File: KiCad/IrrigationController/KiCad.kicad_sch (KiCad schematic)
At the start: 115 parts, among them IC1 MCP23017-E_SO, IC2 MCP23017-E_SO, IC3 DS89C21TMX_NOPB, J1 Screw_Terminal_01x03, J10 Screw_Terminal_01x05, J11 Screw_Terminal_01x02, J12 Screw_Terminal_01x02, J13 Screw_Terminal_01x04, J14 Screw_Terminal_01x02, J15 Screw_Terminal_01x02, J16 Screw_Terminal_01x02, J17 Screw_Terminal_01x02, J18 Screw_Terminal_01x02, J19 Screw_Terminal_01x02, J2 Screw_Terminal_01x03, J21 Screw_Terminal_01x06, J3 Screw_Terminal_01x03, J5 Screw_Terminal_01x03, J6 Screw_Terminal_01x02, J7 Screw_Terminal_01x02, J8 Screw_Terminal_01x02, J9 Screw_Terminal_01x02, K1 2071556-9, K2 2071556-9, Q1 MMBT3906, Q11 MMBT3904, Q12 MMBT3904, Q2 MMBT3906, Q3 MMBT3906, Q6 MMBT3904, Q7 MMBT3904, Q8 MMBT3904, SW1 SW_Push, U1 L298P, U2 ARDUINO_MKR_WAN_1310, U3 L298P, U4 L298P, U5 L298P, U7 L7805

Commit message: PCB created
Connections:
- net COM_1: now also J15.1 (Pin_1); no longer J15.2 (Pin_2)
- net COM_2: now also J16.1 (Pin_1); no longer J16.2 (Pin_2)
- net NO_1: now also J15.2 (Pin_2); no longer J15.1 (Pin_1)
- net NO_2: now also J16.2 (Pin_2); no longer J16.1 (Pin_1)
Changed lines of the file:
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@@
     (effects (font (size 1.27 1.27)) (justify left bottom))
-  )
-  (label "COM_1" (at 384.81 34.29 270) (fields_autoplaced)
-    (effects (font (size 1.27 1.27)) (justify right bottom))
   )
   (label "W2_IN1" (at 120.65 247.65 0) (fields_autoplaced)
@@
     (effects (font (size 1.27 1.27)) (justify left bottom))
   )
+  (label "NO_1" (at 384.81 34.29 270) (fields_autoplaced)
+    (effects (font (size 1.27 1.27)) (justify right bottom))
+  )
   (label "R1_EN" (at 85.09 240.03 180) (fields_autoplaced)
     (effects (font (size 1.27 1.27)) (justify right bottom))
@@
     (effects (font (size 1.27 1.27)) (justify left bottom))
   )
-  (label "COM_2" (at 400.05 34.29 270) (fields_autoplaced)
-    (effects (font (size 1.27 1.27)) (justify right bottom))
-  )
   (label "COM_2" (at 170.18 269.24 0) (fields_autoplaced)
     (effects (font (size 1.27 1.27)) (justify left bottom))
@@
     (effects (font (size 1.27 1.27)) (justify right bottom))
   )
+  (label "COM_2" (at 397.51 34.29 270) (fields_autoplaced)
+    (effects (font (size 1.27 1.27)) (justify right bottom))
+  )
   (label "P1_IN1" (at 328.93 132.08 90) (fields_autoplaced)
     (effects (font (size 1.27 1.27)) (justify left bottom))
@@
     (effects (font (size 1.27 1.27)) (justify right bottom))
   )
-  (label "NO_1" (at 382.27 34.29 270) (fields_autoplaced)
-    (effects (font (size 1.27 1.27)) (justify right bottom))
-  )
   (label "D0-" (at 269.24 275.59 180) (fields_autoplaced)
     (effects (font (size 1.27 1.27)) (justify right bottom))
@@
     (effects (font (size 1.27 1.27)) (justify right bottom))
   )
-  (label "NO_2" (at 397.51 34.29 270) (fields_autoplaced)
-    (effects (font (size 1.27 1.27)) (justify right bottom))
-  )
   (label "PULSE_IN" (at 110.49 49.53 0) (fields_autoplaced)
     (effects (font (size 1.27 1.27)) (justify left bottom))
@@
     (effects (font (size 1.27 1.27)) (justify right bottom))
   )
+  (label "NO_2" (at 400.05 34.29 270) (fields_autoplaced)
+    (effects (font (size 1.27 1.27)) (justify right bottom))
+  )
   (label "RELAY_2_EN" (at 120.65 242.57 0) (fields_autoplaced)
     (effects (font (size 1.27 1.27)) (justify left bottom))
@@
     (effects (font (size 1.27 1.27)) (justify left bottom))
   )
+  (label "COM_1" (at 382.27 34.29 270) (fields_autoplaced)
+    (effects (font (size 1.27 1.27)) (justify right bottom))
+  )
   (label "SDA" (at 91.44 54.61 0) (fields_autoplaced)

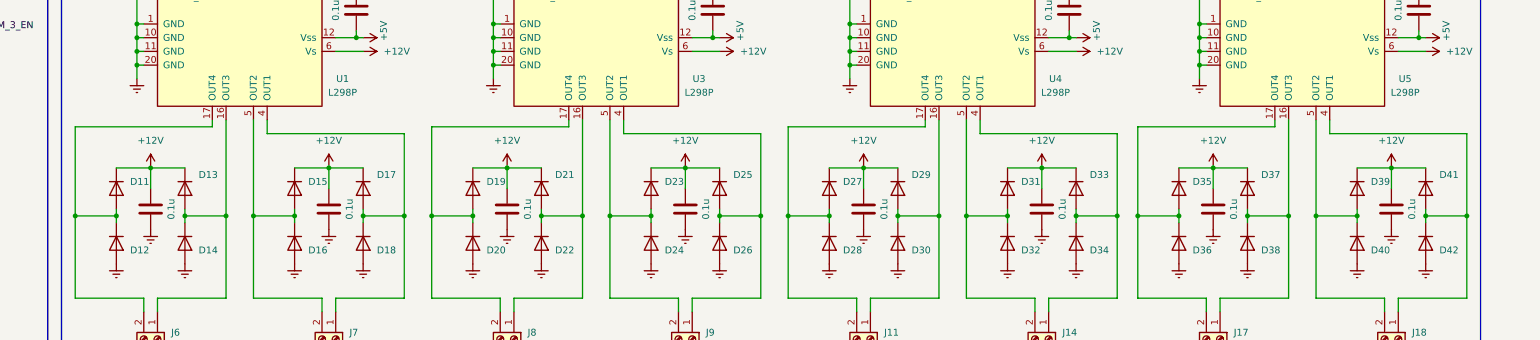
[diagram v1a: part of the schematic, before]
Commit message: L298 as Power
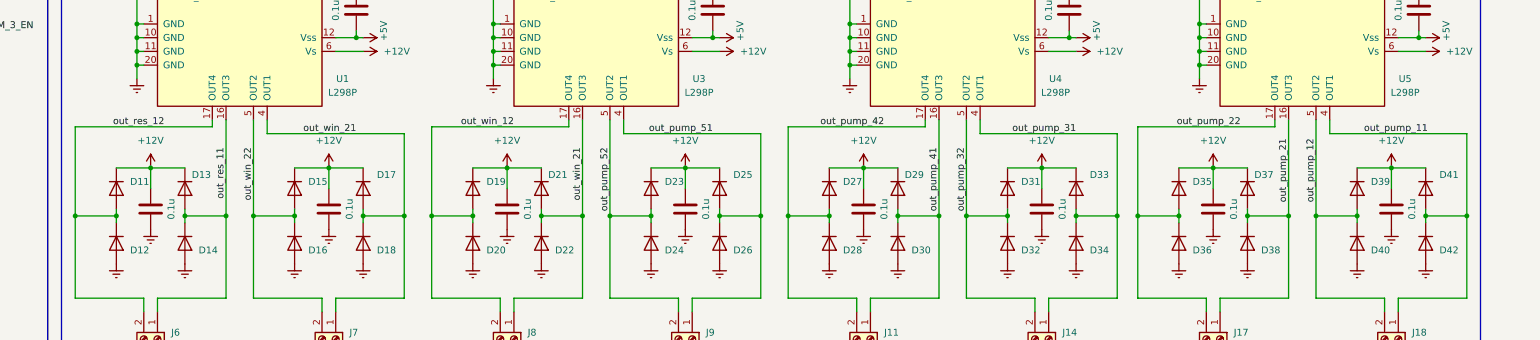
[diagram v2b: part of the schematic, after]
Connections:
- net out_pump_41: now reaches D29.2 (A), D30.1 (K), J11.1 (Pin_1), U4.16 (OUT3)
- net out_win_21: now reaches D17.2 (A), D18.1 (K), J7.1 (Pin_1), U1.4 (OUT1)
- net out_win_21: now also D21.2 (A), D22.1 (K), J8.1 (Pin_1), U3.16 (OUT3)
- net out_win_22: now reaches D15.2 (A), D16.1 (K), J7.2 (Pin_2), U1.5 (OUT2)
- net out_pump_21: now reaches D37.2 (A), D38.1 (K), J17.1 (Pin_1), U5.16 (OUT3)
- net out_win_12: now reaches D19.2 (A), D20.1 (K), J8.2 (Pin_2), U3.17 (OUT4)
- net out_pump_11: now reaches D41.2 (A), D42.1 (K), J18.1 (Pin_1), U5.4 (OUT1)
- net out_res_11: now reaches D13.2 (A), D14.1 (K), J6.1 (Pin_1), U1.16 (OUT3)
- net out_pump_12: now reaches D39.2 (A), D40.1 (K), J18.2 (Pin_2), U5.5 (OUT2)
- net out_pump_22: now reaches D35.2 (A), D36.1 (K), J17.2 (Pin_2), U5.17 (OUT4)
- net out_res_12: now reaches D11.2 (A), D12.1 (K), J6.2 (Pin_2), U1.17 (OUT4)
- net out_pump_42: now reaches D27.2 (A), D28.1 (K), J11.2 (Pin_2), U4.17 (OUT4)
- net out_pump_51: now reaches D25.2 (A), D26.1 (K), J9.1 (Pin_1), U3.4 (OUT1)
- net out_pump_52: now reaches D23.2 (A), D24.1 (K), J9.2 (Pin_2), U3.5 (OUT2)
- net out_pump_32: now reaches D31.2 (A), D32.1 (K), J14.2 (Pin_2), U4.5 (OUT2)
- net out_pump_31: now reaches D33.2 (A), D34.1 (K), J14.1 (Pin_1), U4.4 (OUT1)
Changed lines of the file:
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@@
     (stroke (width 0) (type default))
   )
-  (wire (pts (xy 323.85 170.18) (xy 349.25 170.18))
-    (stroke (width 0) (type default))
-  )
   (wire (pts (xy 240.03 240.03) (xy 240.03 241.3))
     (stroke (width 0) (type default))
@@
     (stroke (width 0) (type default))
   )
+  (wire (pts (xy 316.23 167.64) (xy 316.23 185.42))
+    (stroke (width 0) (type default))
+  )
   (wire (pts (xy 234.95 144.78) (xy 236.22 144.78))
     (stroke (width 0) (type default))
@@
     (stroke (width 0) (type default))
   )
-  (wire (pts (xy 218.44 200.66) (xy 205.74 200.66))
+  (wire (pts (xy 323.85 170.18) (xy 349.25 170.18))
     (stroke (width 0) (type default))
   )
-  (wire (pts (xy 256.54 167.64) (xy 256.54 185.42))
+  (wire (pts (xy 218.44 200.66) (xy 205.74 200.66))
     (stroke (width 0) (type default))
   )
@@
     (stroke (width 0) (type default))
   )
-  (wire (pts (xy 316.23 167.64) (xy 316.23 185.42))
-    (stroke (width 0) (type default))
-  )
   (wire (pts (xy 203.2 29.21) (xy 201.93 29.21))
     (stroke (width 0) (type default))
@@
     (stroke (width 0) (type default))
   )
+  (wire (pts (xy 256.54 167.64) (xy 256.54 185.42))
+    (stroke (width 0) (type default))
+  )
   (wire (pts (xy 124.46 185.42) (xy 124.46 200.66))
     (stroke (width 0) (type default))
@@
     (effects (font (size 1.27 1.27)) (justify left bottom))
   )
+  (label "out_pump_41" (at 251.46 172.72 270) (fields_autoplaced)
+    (effects (font (size 1.27 1.27)) (justify right bottom))
+  )
   (label "P5_EN" (at 62.23 247.65 0) (fields_autoplaced)
     (effects (font (size 1.27 1.27)) (justify left bottom))
@@
     (effects (font (size 1.27 1.27)) (justify left bottom))
   )
+  (label "out_pump_22" (at 307.34 168.91 180) (fields_autoplaced)
+    (effects (font (size 1.27 1.27)) (justify right bottom))
+  )
   (label "RI+" (at 307.34 36.83 90) (fields_autoplaced)
     (effects (font (size 1.27 1.27)) (justify left bottom))
@@
     (effects (font (size 1.27 1.27)) (justify right bottom))
   )
+  (label "out_pump_31" (at 276.86 170.18 180) (fields_autoplaced)
+    (effects (font (size 1.27 1.27)) (justify right bottom))
+  )
   (label "S_HUM_3_EN" (at 110.49 59.69 0) (fields_autoplaced)
     (effects (font (size 1.27 1.27)) (justify left bottom))
@@
     (effects (font (size 1.27 1.27)) (justify left bottom))
   )
+  (label "out_res_12" (at 107.95 168.91 180) (fields_autoplaced)
+    (effects (font (size 1.27 1.27)) (justify right bottom))
+  )
   (label "W2_IN1" (at 132.08 132.08 90) (fields_autoplaced)
     (effects (font (size 1.27 1.27)) (justify left bottom))
@@
     (effects (font (size 1.27 1.27)) (justify left bottom))
   )
+  (label "out_pump_52" (at 190.5 172.72 270) (fields_autoplaced)
+    (effects (font (size 1.27 1.27)) (justify right bottom))
+  )
   (label "FOCO_4_EN" (at 110.49 67.31 0) (fields_autoplaced)
     (effects (font (size 1.27 1.27)) (justify left bottom))
@@
     (effects (font (size 1.27 1.27)) (justify left bottom))
   )
+  (label "out_pump_11" (at 330.2 170.18 0) (fields_autoplaced)
+    (effects (font (size 1.27 1.27)) (justify left bottom))
+  )
+  (label "out_win_21" (at 143.51 170.18 180) (fields_autoplaced)
+    (effects (font (size 1.27 1.27)) (justify right bottom))
+  )
   (label "P2_EN" (at 26.67 247.65 180) (fields_autoplaced)
     (effects (font (size 1.27 1.27)) (justify right bottom))
@@
     (effects (font (size 1.27 1.27)) (justify right bottom))
   )
+  (label "out_pump_42" (at 241.3 168.91 180) (fields_autoplaced)
+    (effects (font (size 1.27 1.27)) (justify right bottom))
+  )
   (label "R1_IN2" (at 85.09 245.11 180) (fields_autoplaced)
     (effects (font (size 1.27 1.27)) (justify right bottom))
@@
     (effects (font (size 1.27 1.27)) (justify right bottom))
   )
+  (label "out_res_11" (at 119.38 172.72 270) (fields_autoplaced)
+    (effects (font (size 1.27 1.27)) (justify right bottom))
+  )
+  (label "out_pump_32" (at 256.54 172.72 270) (fields_autoplaced)
+    (effects (font (size 1.27 1.27)) (justify right bottom))
+  )
   (label "P5_IN1" (at 62.23 245.11 0) (fields_autoplaced)
     (effects (font (size 1.27 1.27)) (justify left bottom))
   )
+  (label "out_pump_51" (at 209.55 170.18 180) (fields_autoplaced)
+    (effects (font (size 1.27 1.27)) (justify right bottom))
+  )
   (label "P3_IN1" (at 264.16 132.08 90) (fields_autoplaced)
     (effects (font (size 1.27 1.27)) (justify left bottom))
   )
+  (label "out_pump_12" (at 321.31 182.88 90) (fields_autoplaced)
+    (effects (font (size 1.27 1.27)) (justify left bottom))
+  )
   (label "W1_IN1" (at 120.65 255.27 0) (fields_autoplaced)
     (effects (font (size 1.27 1.27)) (justify left bottom))
@@
     (effects (font (size 1.27 1.27)) (justify right bottom))
   )
+  (label "out_win_12" (at 172.72 168.91 180) (fields_autoplaced)
+    (effects (font (size 1.27 1.27)) (justify right bottom))
+  )
   (label "NO_2" (at 400.05 34.29 270) (fields_autoplaced)
     (effects (font (size 1.27 1.27)) (justify right bottom))
@@
     (effects (font (size 1.27 1.27)) (justify left bottom))
   )
+  (label "out_win_22" (at 124.46 172.72 270) (fields_autoplaced)
+    (effects (font (size 1.27 1.27)) (justify right bottom))
+  )
   (label "COM_1" (at 382.27 34.29 270) (fields_autoplaced)
     (effects (font (size 1.27 1.27)) (justify right bottom))
   )
+  (label "out_pump_21" (at 316.23 182.88 90) (fields_autoplaced)
+    (effects (font (size 1.27 1.27)) (justify left bottom))
+  )
   (label "SDA" (at 91.44 54.61 0) (fields_autoplaced)
     (effects (font (size 1.27 1.27)) (justify left bottom))
@@
     (effects (font (size 1.27 1.27)) (justify left bottom))
   )
+  (label "out_win_21" (at 185.42 172.72 270) (fields_autoplaced)
+    (effects (font (size 1.27 1.27)) (justify right bottom))
+  )
   (symbol (lib_id "power:Earth") (at 243.84 194.31 0) (unit 1)
     (in_bom yes) (on_board yes) (dnp no) (fields_autoplaced)
@@
   (symbol (lib_id "Diode:1N4007") (at 111.76 180.34 270) (unit 1)
     (in_bom yes) (on_board yes) (dnp no)
-    (property "Reference" "D13" (at 114.3 177.8 90)
+    (property "Reference" "D13" (at 113.03 177.8 90)
       (effects (font (size 1.27 1.27)) (justify left))
     )
@@
   (symbol (lib_id "Diode:1N4007") (at 243.84 180.34 270) (unit 1)
     (in_bom yes) (on_board yes) (dnp no)
-    (property "Reference" "D29" (at 246.38 177.8 90)
+    (property "Reference" "D29" (at 245.11 177.8 90)
       (effects (font (size 1.27 1.27)) (justify left))
     )
@@
   (symbol (lib_id "Diode:1N4007") (at 308.61 180.34 270) (unit 1)
     (in_bom yes) (on_board yes) (dnp no)
-    (property "Reference" "D37" (at 311.15 177.8 90)
+    (property "Reference" "D37" (at 309.88 177.8 90)
       (effects (font (size 1.27 1.27)) (justify left))
     )
@@
   (symbol (lib_id "Diode:1N4007") (at 177.8 180.34 270) (unit 1)
     (in_bom yes) (on_board yes) (dnp no)
-    (property "Reference" "D21" (at 180.34 177.8 90)
+    (property "Reference" "D21" (at 179.07 177.8 90)
       (effects (font (size 1.27 1.27)) (justify left))
     )

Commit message: qwer
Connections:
- net FOCO_1_EN: now also J10.4 (Pin_4); no longer J10.1 (Pin_1)
- net FOCO_2_EN: now also J10.3 (Pin_3); no longer J10.2 (Pin_2)
- net FOCO_3_EN: now also J10.2 (Pin_2); no longer J10.3 (Pin_3)
- net FOCO_4_EN: now also J10.1 (Pin_1); no longer J10.4 (Pin_4)
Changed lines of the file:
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@@
+    (stroke (width 0) (type default))
+  )
+  (wire (pts (xy 332.74 34.29) (xy 332.74 31.75))
     (stroke (width 0) (type default))
   )
@@
     (stroke (width 0) (type default))
   )
+  (wire (pts (xy 327.66 34.29) (xy 327.66 31.75))
+    (stroke (width 0) (type default))
+  )
   (wire (pts (xy 276.86 184.15) (xy 276.86 185.42))
     (stroke (width 0) (type default))
@@
     (stroke (width 0) (type default))
   )
-  (wire (pts (xy 325.12 34.29) (xy 325.12 31.75))
-    (stroke (width 0) (type default))
-  )
   (wire (pts (xy 326.39 132.08) (xy 326.39 137.16))
     (stroke (width 0) (type default))
@@
     (stroke (width 0) (type default))
   )
+  (wire (pts (xy 330.2 34.29) (xy 330.2 31.75))
+    (stroke (width 0) (type default))
+  )
   (wire (pts (xy 234.95 154.94) (xy 234.95 157.48))
     (stroke (width 0) (type default))
@@
     (stroke (width 0) (type default))
   )
-  (wire (pts (xy 332.74 34.29) (xy 332.74 31.75))
+  (wire (pts (xy 325.12 31.75) (xy 325.12 34.29))
     (stroke (width 0) (type default))
   )
@@
     (stroke (width 0) (type default))
   )
-  (wire (pts (xy 330.2 34.29) (xy 330.2 31.75))
-    (stroke (width 0) (type default))
-  )
   (wire (pts (xy 191.77 57.15) (xy 207.01 57.15))
     (stroke (width 0) (type default))
@@
   )
   (wire (pts (xy 276.86 275.59) (xy 283.21 275.59))
-    (stroke (width 0) (type default))
-  )
-  (wire (pts (xy 327.66 34.29) (xy 327.66 31.75))
     (stroke (width 0) (type default))
   )
@@
     (effects (font (size 1.27 1.27)) (justify left bottom))
   )
-  (label "FOCO_2_EN" (at 327.66 34.29 270) (fields_autoplaced)
-    (effects (font (size 1.27 1.27)) (justify right bottom))
-  )
   (label "Vin" (at 196.85 24.13 180) (fields_autoplaced)
     (effects (font (size 1.27 1.27)) (justify right bottom))
@@
     (effects (font (size 1.27 1.27)) (justify left bottom))
   )
+  (label "FOCO_1_EN" (at 332.74 34.29 270) (fields_autoplaced)
+    (effects (font (size 1.27 1.27)) (justify right bottom))
+  )
   (label "S_ANEM_IN" (at 40.64 198.12 0) (fields_autoplaced)
     (effects (font (size 1.27 1.27)) (justify left bottom))
@@
     (effects (font (size 1.27 1.27)) (justify right bottom))
   )
+  (label "FOCO_4_EN" (at 325.12 34.29 270) (fields_autoplaced)
+    (effects (font (size 1.27 1.27)) (justify right bottom))
+  )
   (label "FOCO_4_EN" (at 110.49 67.31 0) (fields_autoplaced)
     (effects (font (size 1.27 1.27)) (justify left bottom))
@@
     (effects (font (size 1.27 1.27)) (justify left bottom))
   )
-  (label "FOCO_3_EN" (at 330.2 34.29 270) (fields_autoplaced)
-    (effects (font (size 1.27 1.27)) (justify right bottom))
-  )
   (label "D0+" (at 269.24 278.13 180) (fields_autoplaced)
     (effects (font (size 1.27 1.27)) (justify right bottom))
@@
     (effects (font (size 1.27 1.27)) (justify right bottom))
   )
+  (label "FOCO_2_EN" (at 330.2 34.29 270) (fields_autoplaced)
+    (effects (font (size 1.27 1.27)) (justify right bottom))
+  )
   (label "P5_IN2" (at 200.66 132.08 90) (fields_autoplaced)
     (effects (font (size 1.27 1.27)) (justify left bottom))
@@
     (effects (font (size 1.27 1.27)) (justify left bottom))
   )
-  (label "FOCO_1_EN" (at 325.12 34.29 270) (fields_autoplaced)
+  (label "FOCO_3_EN" (at 327.66 34.29 270) (fields_autoplaced)
     (effects (font (size 1.27 1.27)) (justify right bottom))
   )
@@
     (effects (font (size 1.27 1.27)) (justify left bottom))
   )
-  (label "FOCO_4_EN" (at 332.74 34.29 270) (fields_autoplaced)
-    (effects (font (size 1.27 1.27)) (justify right bottom))
-  )
   (label "R1_IN2" (at 124.46 132.08 90) (fields_autoplaced)

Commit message: tracing in controller
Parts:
- removed TP1, TP2: TestPoint, TestPoint:TestPoint_Pad_2.0x2.0mm, symbol Connector:TestPoint
- added J4: Conn_01x04_Pin, Connector_PinHeader_2.54mm:PinHeader_1x04_P2.54mm_Vertical, symbol Connector:Conn_01x04_Pin
- renumbered K2 to K1, K1 to K2
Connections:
- net +3.3V: now also C16.1, C17.1
- net +5V: now also J4.4 (Pin_4); no longer C16.1, C17.1
- net Earth: now also J4.1 (Pin_1)
- net P3_EN: now also IC1.25 (GPA4); no longer IC1.7 (GPB6)
- net P3_IN1: now also IC1.26 (GPA5); no longer IC1.8 (GPB7)
- net P3_IN2: now also IC1.27 (GPA6); no longer IC1.21 (GPA0)
- net P5_EN: now also IC1.21 (GPA0); no longer IC1.25 (GPA4)
- net P5_IN1: now also IC1.7 (GPB6); no longer IC1.26 (GPA5)
- net P5_IN2: now also IC1.8 (GPB7); no longer IC1.27 (GPA6)
- net PULSE_IN: now also U2.J3_13 (PB10/D4(PWM)); no longer U2.J3_7 (PA06/D20/AIN(6)/A5)
- net RELAY_1_EN: now also IC2.7 (GPB6); no longer IC2.28 (GPA7)
- net RELAY_2_EN: now also IC2.8 (GPB7); no longer IC2.27 (GPA6)
- net RX: now also J4.3 (Pin_3)
- net TX: now also J4.2 (Pin_2)
- net W1_EN: now also IC2.24 (GPA3); no longer IC2.21 (GPA0)
- net W1_IN1: now also IC2.25 (GPA4); no longer IC2.22 (GPA1)
- net W1_IN2: now also IC2.26 (GPA5); no longer IC2.23 (GPA2)
- net W2_EN: now also IC2.21 (GPA0); no longer IC2.24 (GPA3)
- net W2_IN1: now also IC2.22 (GPA1); no longer IC2.25 (GPA4)
- net W2_IN2: now also IC2.23 (GPA2); no longer IC2.26 (GPA5)

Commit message: qwer
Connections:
- net out_win_21: no longer D21.2 (A), D22.1 (K), J8.1 (Pin_1), U3.16 (OUT3)
- new net out_win_11: D21.2 (A), D22.1 (K), J8.1 (Pin_1), U3.16 (OUT3)
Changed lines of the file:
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@@
     (effects (font (size 1.27 1.27)) (justify left bottom))
   )
-  (label "out_win_21" (at 185.42 172.72 270) (fields_autoplaced)
+  (label "out_win_11" (at 185.42 172.72 270) (fields_autoplaced)
     (effects (font (size 1.27 1.27)) (justify right bottom))
   )
